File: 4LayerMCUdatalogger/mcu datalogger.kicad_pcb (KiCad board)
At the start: 4 copper layers, 50.3 x 32 mm, 29 parts, among them J1 Conn_01x04_Pin, J2 Conn_01x09_Pin, J3 Conn_01x04_Pin, J4 Conn_02x03_Odd_Even, U1 24LC1025, U2 DS1337S_, U3 24LC1025, U4 ATMEGA328P-AU, Y1 32.768 KHz, Y2 16MHz

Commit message: Small modifications.
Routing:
- net /SCL: track 75.8 -> 75.2 mm
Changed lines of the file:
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@@
       (drillshape 0)
       (scaleselection 1)
-      (outputdirectory "mcu datalogger gerbers/")
+      (outputdirectory "4layer_MCU_Datalogger_gerbers/")
     )
   )
@@
   (segment (start 145.764 85.7615) (end 145.764 76.2365) (width 0.25) (layer "In2.Cu") (net 8))
   (segment (start 129.2233 74.7072) (end 129.2233 72.9038) (width 0.25) (layer "In2.Cu") (net 8))
-  (segment (start 115.725738 78.8372) (end 116.1732 78.8372) (width 0.25) (layer "F.Cu") (net 9))
   (segment (start 114.9079 78.8372) (end 114.2627 79.4824) (width 0.25) (layer "F.Cu") (net 9))
   (segment (start 114.5167 85.057126) (end 115.738974 86.2794) (width 0.25) (layer "F.Cu") (net 9))
@@
   (segment (start 134.8875 72.4212) (end 134.8875 72.2688) (width 0.25) (layer "F.Cu") (net 9))
   (segment (start 136.9149 72.5298) (end 135.1485 72.5298) (width 0.25) (layer "F.Cu") (net 9))
+  (segment (start 113.8055 77.1456) (end 115.4971 78.8372) (width 0.25) (layer "F.Cu") (net 9))
+  (segment (start 115.4971 78.8372) (end 115.725738 78.8372) (width 0.25) (layer "F.Cu") (net 9))
   (segment (start 115.4413 70.9124) (end 114.3135 72.0402) (width 0.25) (layer "F.Cu") (net 9))
   (segment (start 127.038 73.1686) (end 127.038 73.780227) (width 0.25) (layer "F.Cu") (net 9))
   (segment (start 120.6889 73.0054) (end 118.5959 70.9124) (width 0.25) (layer "F.Cu") (net 9))
-  (segment (start 113.8055 76.663) (end 115.725738 78.8372) (width 0.25) (layer "F.Cu") (net 9))
   (segment (start 137.9899 73.6048) (end 136.9149 72.5298) (width 0.25) (layer "F.Cu") (net 9))
   (segment (start 135.0399 72.4212) (end 134.8875 72.4212) (width 0.25) (layer "F.Cu") (net 9))
+  (segment (start 113.8055 76.663) (end 113.8055 77.1456) (width 0.25) (layer "F.Cu") (net 9))
   (segment (start 134.8875 72.2688) (end 134.9129 72.2942) (width 0.25) (layer "F.Cu") (net 9))
   (segment (start 146.6027 90.0684) (end 149.3266 90.0684) (width 0.25) (layer "F.Cu") (net 9))
@@
   (segment (start 113.8055 76.663) (end 113.8055 72.5736) (width 0.25) (layer "In1.Cu") (net 9))
   (segment (start 129.7567 72.4212) (end 134.8875 72.4212) (width 0.25) (layer "In1.Cu") (net 9))
-  (segment (start 114.5167 84.8926) (end 114.2627 84.7148) (width 0.25) (layer "In1.Cu") (net 9))
   (segment (start 127.3183 74.8596) (end 129.7567 72.4212) (width 0.25) (layer "In1.Cu") (net 9))
   (segment (start 127.3183 74.8596) (end 126.9431 74.4844) (width 0.25) (layer "In2.Cu") (net 9))

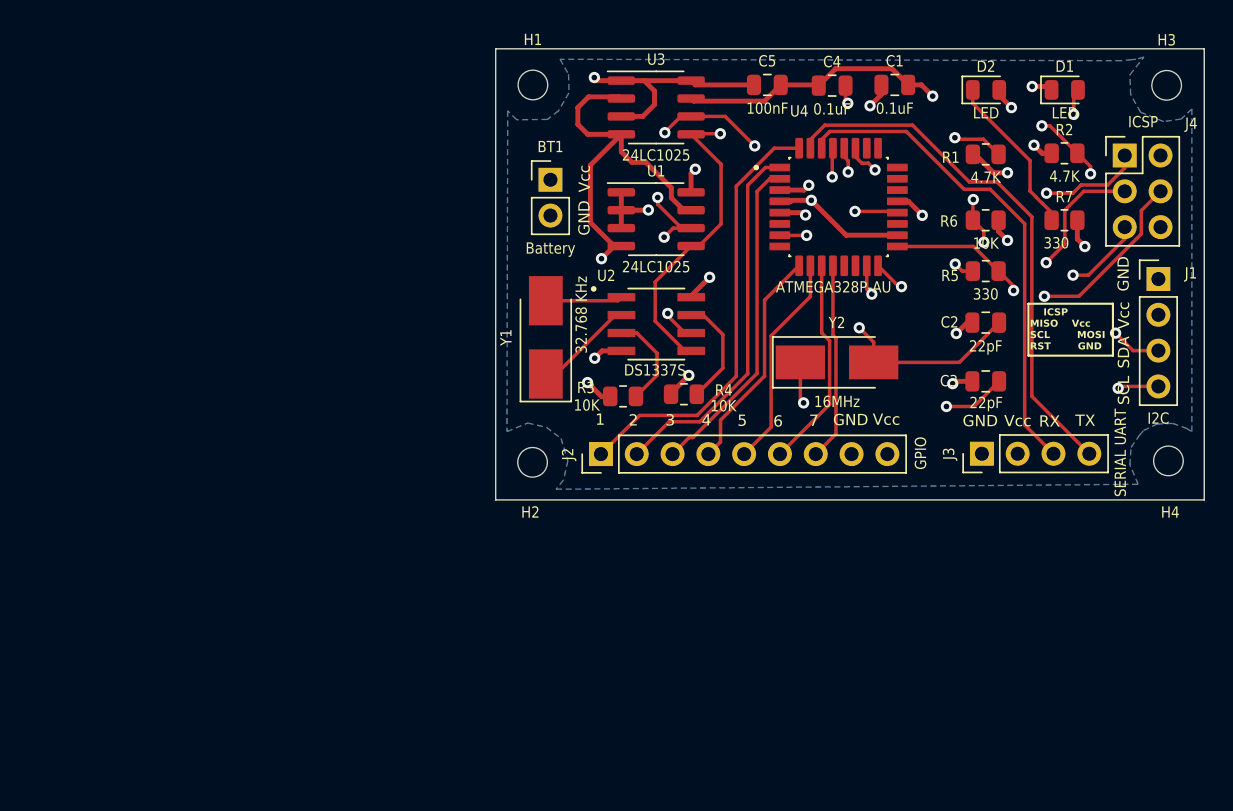
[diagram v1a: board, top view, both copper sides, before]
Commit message: Added Board Characteristics.
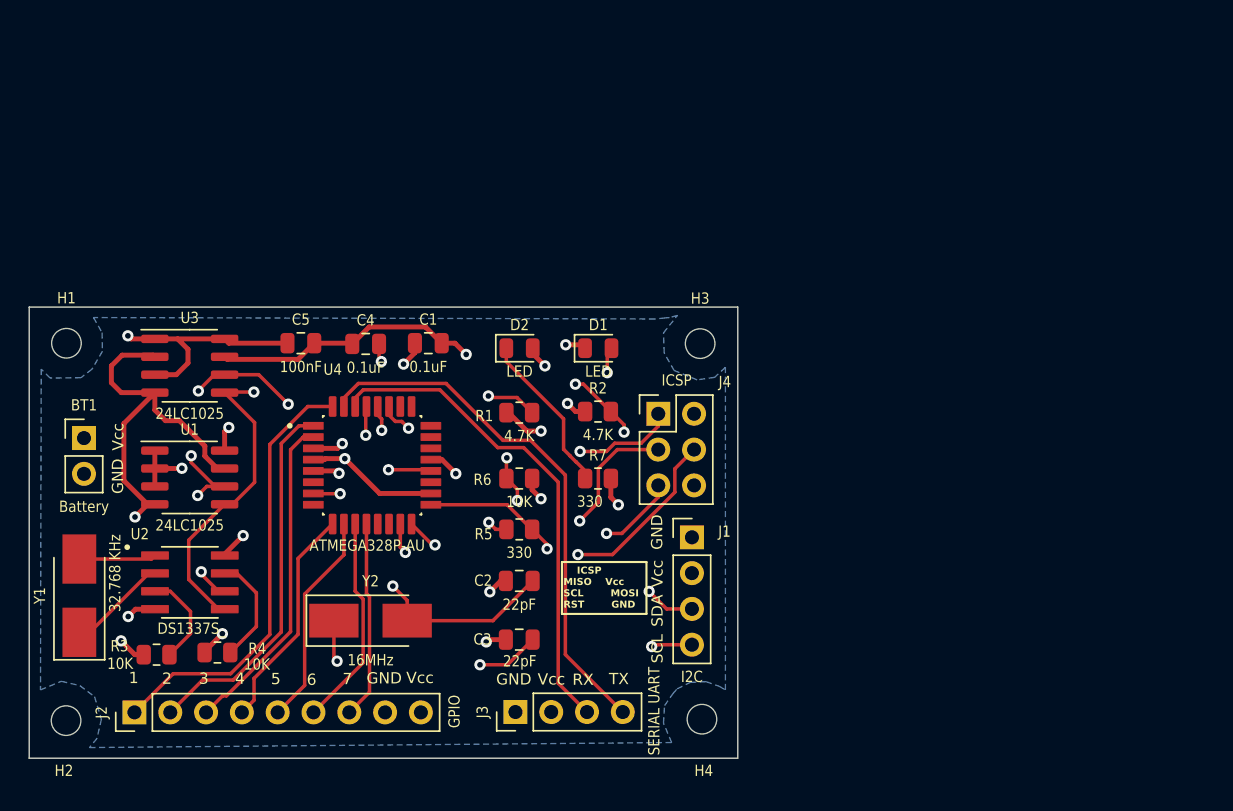
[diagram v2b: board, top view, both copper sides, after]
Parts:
- moved C2 37.8 mm to (104.0, 103.9)
- moved C3 37.8 mm to (104.0, 108.0)
- moved C4 37.8 mm to (93.1, 87.1)
- moved D1 37.8 mm to (109.6, 87.4)
- moved H2 37.8 mm to (71.8, 113.8)
- moved H3 37.8 mm to (116.8, 87.0)
- moved J1 37.8 mm to (116.2, 100.8)
- moved R1 37.8 mm to (104.0, 91.9)
- moved R5 37.8 mm to (104.0, 100.2)
- moved R6 37.8 mm to (104.0, 96.6)
- moved U4 37.8 mm to (93.5, 95.7)
- moved BT1 37.8 mm to (73.1, 93.7)
- moved C1 37.8 mm to (97.5, 87.0)
- moved C5 37.8 mm to (88.5, 87.0)
- moved D2 37.8 mm to (104.0, 87.4)
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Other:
- board text added: "0.2000 mm / 0.0000 mm"
- board text added: "0.3000 mm"
- board text added: "1.6000 mm"
- board text added: "50.2666 mm x 32.0040 mm"
- board text added: "BOARD CHARACTERISTICS"
- board text added: "Board Thickness:"
- board text added: "Board overall dimensions:"
- board text added: "Castellated pads:"
- board text added: "Copper Finish:"
- board text added: "Copper Layer Count:"
- board text added: "Edge card connectors:"
- board text added: "Impedance Control:"
- board text added: "Min hole diameter:"
- board text added: "Min track/spacing:"
- board text added: "No"
- board text added: "None"
- board text added: "Plated Board Edge:"

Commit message: Successfully completed the 4Layer MCU Datalogger PCB project.
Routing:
- net Net-(U4-PB7): track 17.7 -> 26.8 mm, vias 2 -> 4
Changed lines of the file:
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@@
       (layer "F.Mask" (type "Top Solder Mask") (thickness 0.01))
       (layer "F.Cu" (type "copper") (thickness 0.035))
-      (layer "dielectric 1" (type "prepreg") (thickness 0.1) (material "FR4") (epsilon_r 4.5) (loss_tangent 0.02))
+      (layer "dielectric 1" (type "core") (thickness 0.1) (material "FR4") (epsilon_r 4.5) (loss_tangent 0.02))
       (layer "In1.Cu" (type "copper") (thickness 0.035))
-      (layer "dielectric 2" (type "core") (thickness 1.24) (material "FR4") (epsilon_r 4.5) (loss_tangent 0.02))
+      (layer "dielectric 2" (type "prepreg") (thickness 1.24) (material "FR4") (epsilon_r 4.5) (loss_tangent 0.02))
       (layer "In2.Cu" (type "copper") (thickness 0.035))
-      (layer "dielectric 3" (type "prepreg") (thickness 0.1) (material "FR4") (epsilon_r 4.5) (loss_tangent 0.02))
+      (layer "dielectric 3" (type "core") (thickness 0.1) (material "FR4") (epsilon_r 4.5) (loss_tangent 0.02))
       (layer "B.Cu" (type "copper") (thickness 0.035))
       (layer "B.Mask" (type "Bottom Solder Mask") (thickness 0.01))
@@
   (segment (start 91.2778 97.679) (end 91.2778 100.4984) (width 0.25) (layer "In1.Cu") (net 3))
   (segment (start 91.2778 100.4984) (end 95.0116 104.2322) (width 0.25) (layer "In1.Cu") (net 3))
+  (segment (start 91.0217 103.9934) (end 90.8331 104.182) (width 0.25) (layer "F.Cu") (net 4))
+  (segment (start 89.3707 99.4468) (end 89.3739 99.4436) (width 0.25) (layer "F.Cu") (net 4))
+  (segment (start 90.8331 104.182) (end 90.8331 106.6858) (width 0.25) (layer "F.Cu") (net 4))
+  (segment (start 89.3739 98.4622) (end 89.3707 99.4468) (width 0.25) (layer "F.Cu") (net 4))
   (segment (start 91.0611 109.5604) (end 90.8331 109.3324) (width 0.25) (layer "F.Cu") (net 4))
   (segment (start 90.8331 109.3324) (end 90.8331 106.6858) (width 0.25) (layer "F.Cu") (net 4))
@@
   (segment (start 103.1509 109.8144) (end 101.1957 109.8144) (width 0.25) (layer "F.Cu") (net 4))
   (via (at 101.1957 109.8144) (size 0.8) (drill 0.4) (layers "F.Cu" "B.Cu") (net 4))
+  (via (at 91.0217 103.9934) (size 0.8) (drill 0.4) (layers "F.Cu" "B.Cu") (net 4))
   (via (at 91.0611 109.5604) (size 0.8) (drill 0.4) (layers "F.Cu" "B.Cu") (net 4))
+  (via (at 89.3707 99.4468) (size 0.8) (drill 0.4) (layers "F.Cu" "B.Cu") (net 4))
+  (segment (start 89.3707 99.4468) (end 89.3707 102.3678) (width 0.25) (layer "In1.Cu") (net 4))
+  (segment (start 91.0217 103.9934) (end 91.0217 104.0188) (width 0.25) (layer "In1.Cu") (net 4))
+  (segment (start 91.0217 104.0188) (end 90.9963 103.9934) (width 0.25) (layer "In1.Cu") (net 4))
+  (segment (start 89.3707 102.3678) (end 90.9963 103.9934) (width 0.25) (layer "In1.Cu") (net 4))
   (segment (start 101.1957 109.8144) (end 91.3151 109.8144) (width 0.25) (layer "In1.Cu") (net 4))
   (segment (start 91.3151 109.8144) (end 91.0611 109.5604) (width 0.25) (layer "In1.Cu") (net 4))
+  (segment (start 90.9963 103.9934) (end 91.0217 103.9934) (width 0.25) (layer "In1.Cu") (net 4))
   (segment (start 94.7068 95.9772) (end 97.6289 95.9772) (width 0.25) (layer "F.Cu") (net 5))
   (segment (start 94.0367 87.0516) (end 94.0367 88.1443) (width 0.25) (layer "F.Cu") (net 5))
